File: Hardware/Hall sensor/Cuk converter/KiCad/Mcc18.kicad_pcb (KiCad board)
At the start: 2 copper layers, 202.2 x 107.2 mm, 47 parts, among them Q1 IRFP4321PbF, U1 LTSP_25-NP, U2 DRIVER_(INEP), U3 LM7812_TO220, U4 Signals_MCC, U5 ZCS

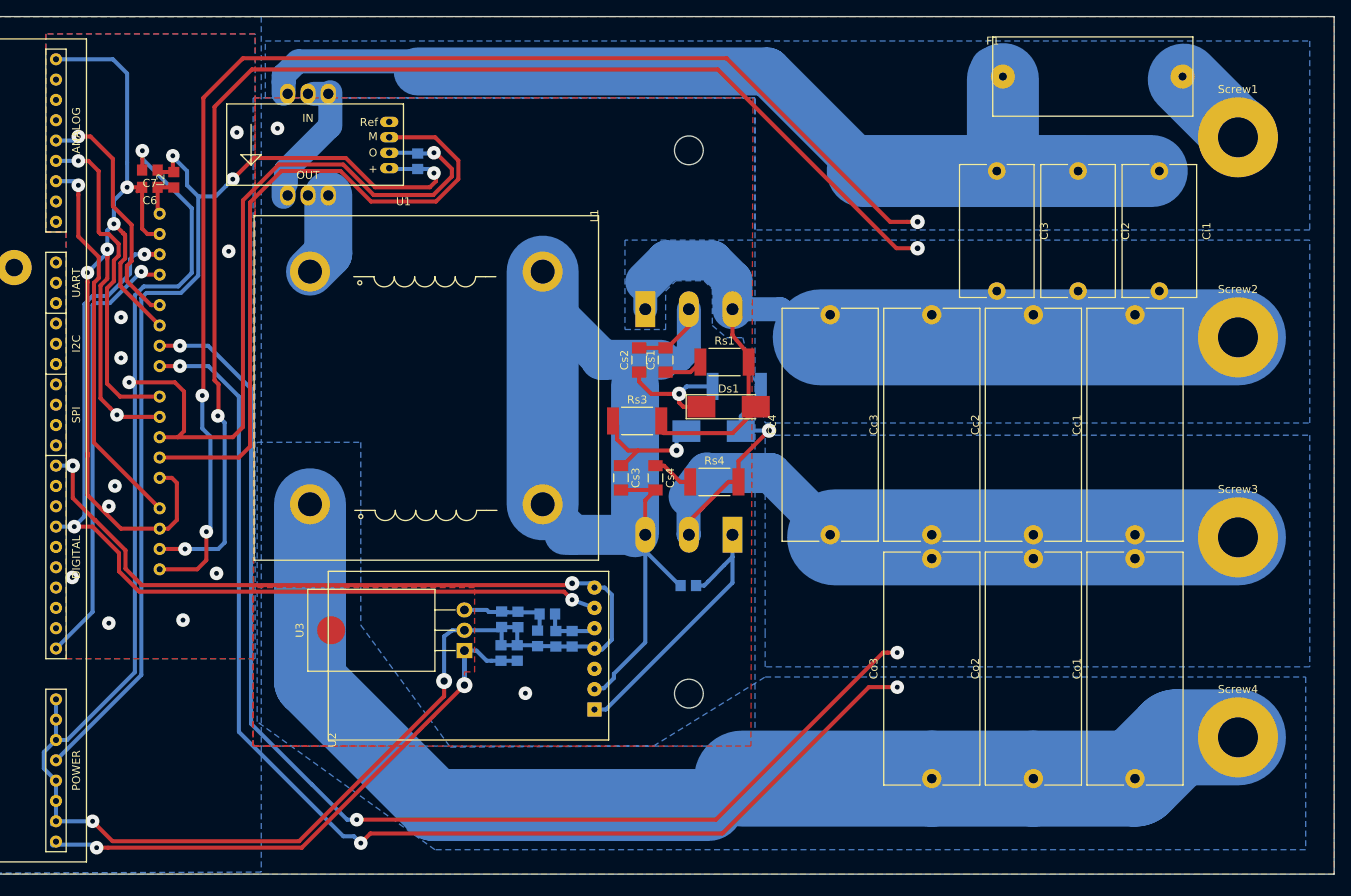
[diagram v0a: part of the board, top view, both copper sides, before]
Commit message: rework on snubber routing
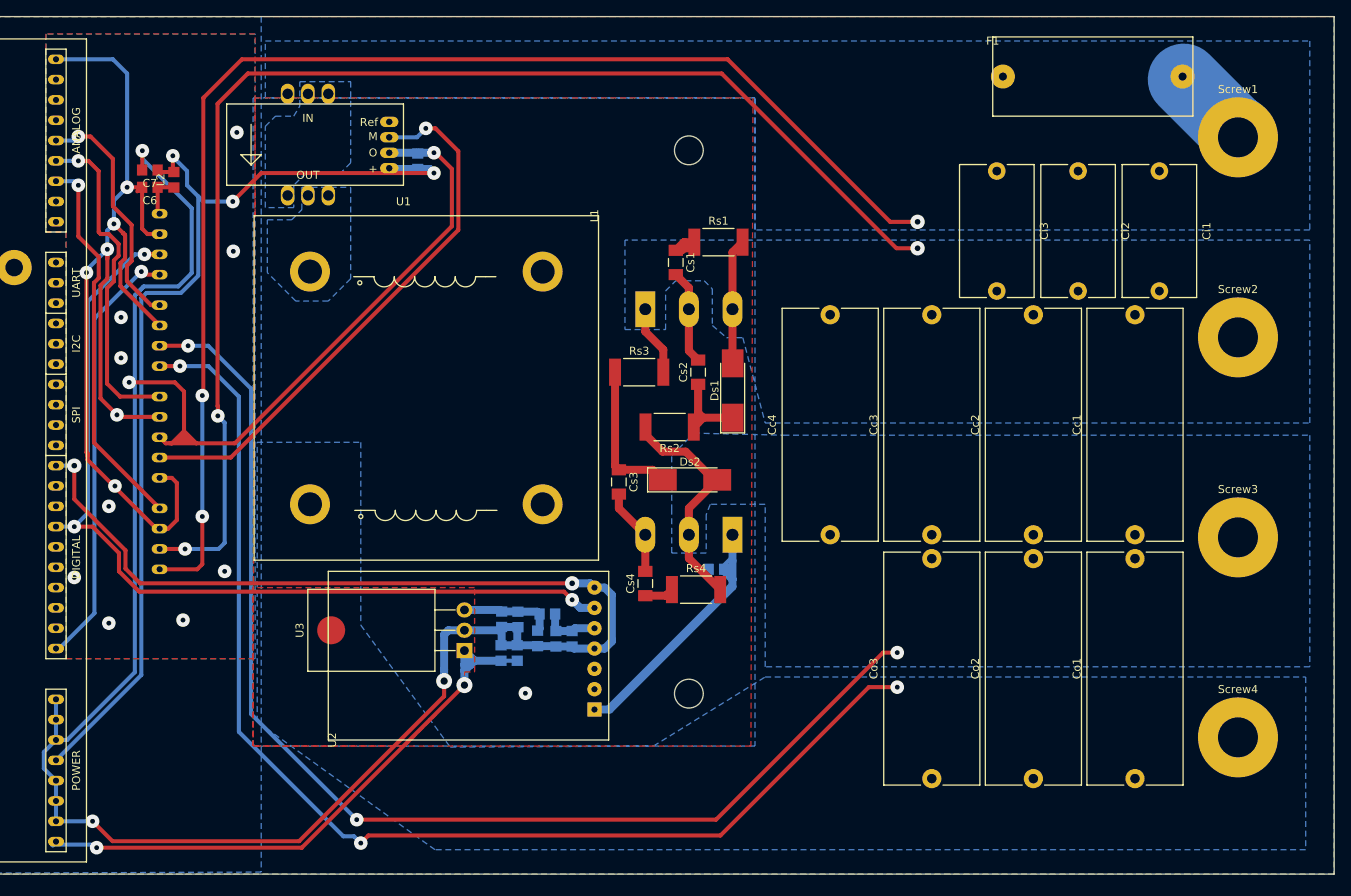
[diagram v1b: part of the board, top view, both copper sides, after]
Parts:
- Ds2, Rs2: moved to F.Cu
- moved HS1 54.6 mm to (208.3, 57.7)
- moved Rs1 15.0 mm to (210.1, 38.1)
- moved Rs4 13.7 mm to (207.3, 81.5)
- moved Cs4 13.3 mm to (200.9, 80.8), turned to 90 degrees
- moved Cs1 12.3 mm to (204.7, 40.6), turned to 270 degrees
- moved Rs2 9.80 mm to (204.0, 61.2), turned to 180 degrees
- moved Cs2 7.52 mm to (207.5, 54.4)
- moved Ds2 6.77 mm to (206.5, 67.8)
- moved Rs3 6.10 mm to (200.2, 54.4)
- moved R1 4.05 mm to (209.8, 79.0)
- moved Ds1 2.09 mm to (211.8, 56.6), turned to 90 degrees
- moved Cs3 0.57 mm to (197.6, 68.1)
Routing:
- net /+B: track 291.9 -> 149.5 mm
- net /-Vp: track 296.9 -> 164.0 mm
- net /Source: track 143.5 -> 22.9 mm, vias 2 -> 1
- net /+Vp: track 275.1 -> 186.3 mm
- net /-B: track 255.7 -> 178.3 mm, vias 4 -> 3
- net /Gate: track 35.9 -> 63.1 mm
- net Net-(U1-Pad3): track 16.2 -> 0.00 mm
- net /Ipanel+: track 84.9 -> 69.2 mm, vias 0 -> 1
- net Net-(L1-Pad1): track 10.5 -> 0.00 mm
- net Net-(Cs2-Pad1): track 15.5 -> 11.8 mm, vias 1 -> 0
- net Net-(Cs3-Pad1): track 15.6 -> 18.4 mm, vias 1 -> 0
- net +5V: track 132.3 -> 129.5 mm
- net /+18V_OUT: track 75.7 -> 78.3 mm
- net GNDA: track 140.4 -> 137.9 mm
- net Net-(Cs4-Pad1): track 5.19 -> 3.65 mm
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- added copper zone on B.Cu, net Net-(L1-Pad1)
- added copper zone on B.Cu, net Net-(U1-Pad3)

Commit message: PCB Reworked
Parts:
- added R101: ??, Resistor_SMD:R_0805_2012Metric_Pad1.29x1.40mm_HandSolder, F.Cu at (187.5, 65.5)
- added R102: ??, Resistor_SMD:R_0805_2012Metric_Pad1.29x1.40mm_HandSolder, F.Cu at (187.5, 68.8)
- added R103: ??, Resistor_SMD:R_0805_2012Metric_Pad1.29x1.40mm_HandSolder, F.Cu at (187.5, 123.4)
- added R104: ??, Resistor_SMD:R_0805_2012Metric_Pad1.29x1.40mm_HandSolder, F.Cu at (187.5, 120.1)
- added R105: 0R, Resistor_SMD:R_0805_2012Metric_Pad1.29x1.40mm_HandSolder, B.Cu at (141.2, 54.9)
- added R106: 0R, Resistor_SMD:R_0805_2012Metric_Pad1.29x1.40mm_HandSolder, B.Cu at (141.2, 56.9)
- moved HS1 103.6 mm to (147.1, 141.2)
- moved C2 52.5 mm to (145.7, 124.5), turned to 0 degrees
- moved L2 50.2 mm to (102.6, 61.5)
- moved C6 50.2 mm to (102.6, 65.8), turned to 270 degrees
- moved C3 49.3 mm to (145.7, 121.9), turned to 0 degrees
- moved C4 47.7 mm to (146.6, 116.0)
- moved C5 47.5 mm to (148.8, 116.0)
- moved C8 46.1 mm to (151.1, 116.0)
- moved Ds2 46.1 mm to (171.7, 98.0)
- moved R1 46.1 mm to (175.0, 109.2)
- moved C7 45.9 mm to (102.6, 57.1), turned to 90 degrees
- moved C1 45.9 mm to (137.7, 58.0)
- moved Rs2 45.9 mm to (169.2, 91.2)
- moved Screw4 45.9 mm to (240.2, 130.0)
- moved U3 45.9 mm to (143.5, 119.1)
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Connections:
- U1 pad 9: /Ipanel+ -> /+Ip
- U4 pad 1: /-Vp -> /Vp_sen-
- U4 pad 10: /+B -> /Vb_sen+
- U4 pad 11: /-B -> /Vb_sen-
- U4 pad 2: /+Vp -> /Vp_sen+
- U4 pad 6: /Ipanel+ -> /Ip_sen+
- U4 pad 7: GND -> /Ip_sen-
- U5 pad 2: GND -> Net-(U5-Pad2)
- U5 pad 4: GND -> Net-(U5-Pad4)
- U5 pad 6: GND -> Net-(U5-Pad6)
- U5 pad 8: GND -> Net-(U5-Pad8)
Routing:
- net /Vp_sen+: track 0.00 -> 172.4 mm
- net /Vp_sen-: track 0.00 -> 169.5 mm
- net /-Vp: track 164.0 -> 2.36 mm, vias 3 -> 1
- net /+Vp: track 186.3 -> 26.8 mm, vias 3 -> 1
- net /Vb_sen-: track 0.00 -> 153.6 mm, vias 0 -> 2
- net /Vb_sen+: track 0.00 -> 153.5 mm, vias 0 -> 2
- net /+B: track 149.5 -> 2.36 mm, vias 3 -> 1
- net /-B: track 178.3 -> 31.4 mm, vias 3 -> 1
- net GNDA: track 137.9 -> 2.92 mm, vias 15 -> 0
- net GND: track 377.7 -> 264.7 mm, vias 7 -> 10
- net /Ip_sen-: track 0.00 -> 94.5 mm, vias 0 -> 3
- net /Ip_sen+: track 0.00 -> 91.3 mm, vias 0 -> 3
- net /Ipanel+: track 69.2 -> 0.00 mm, vias 1 -> 0
- net +5V: track 129.5 -> 188.8 mm
- net +12V: track 11.8 -> 29.9 mm
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- added copper zone on F.Cu, net /+B
- added copper zone on F.Cu, net /+Vp
- added copper zone on F.Cu, net /-B
- added copper zone on F.Cu, net /-Vp
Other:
- board size 202.2 x 107.2 mm -> 199.1 x 107.2 mm
- rule via_min_size: 0.6 -> 0.7

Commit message: minor fixes and added IMG folder
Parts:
- moved R1 24.3 mm to (156.7, 125.2), turned to 270 degrees
- moved Cs4 3.06 mm to (169.2, 111.0)
- moved Rs4 3.05 mm to (175.5, 111.5)
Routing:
- net /Vp_sen-: track 169.5 -> 156.0 mm
- net /Gate: track 49.8 -> 40.7 mm
- net /Vp_sen+: track 172.4 -> 168.7 mm
- net /-B: track 31.4 -> 33.9 mm
- net /Source: track 22.9 -> 23.8 mm

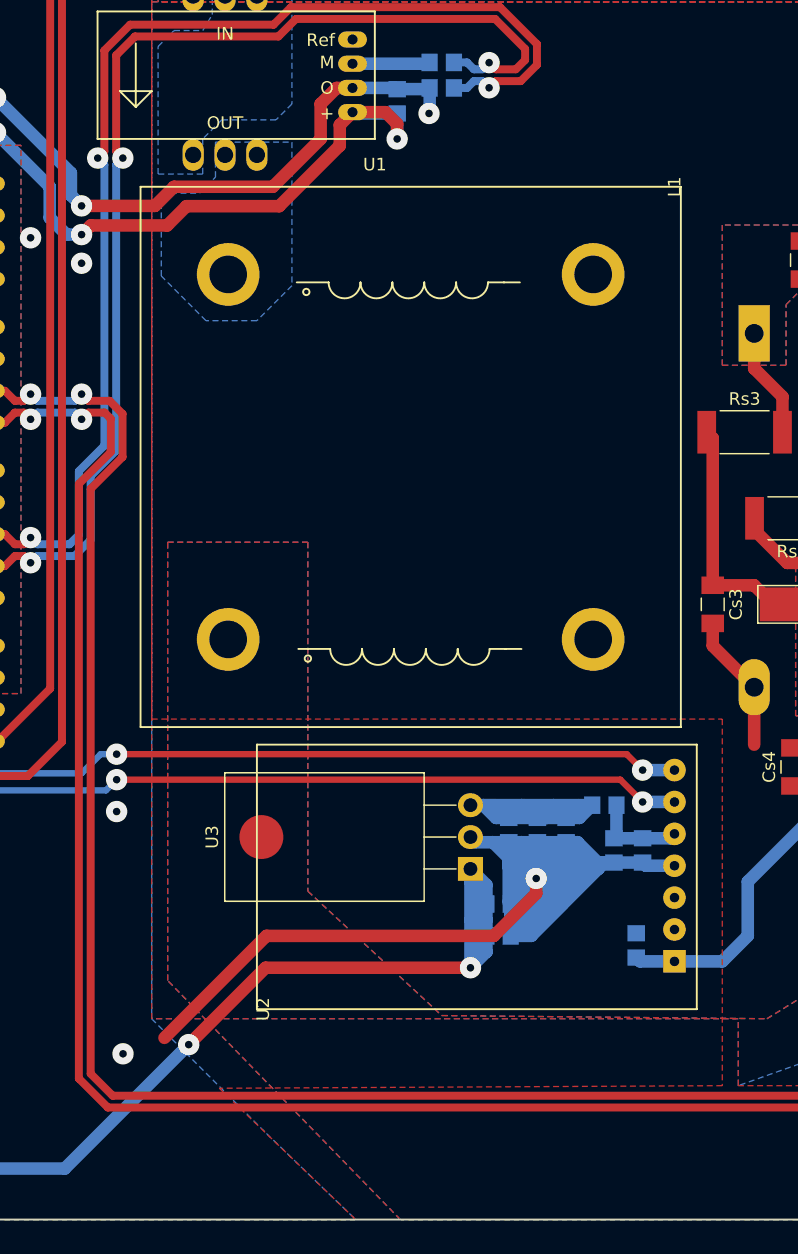
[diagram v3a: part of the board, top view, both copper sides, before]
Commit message: pads and traces of current sensor supply fixed
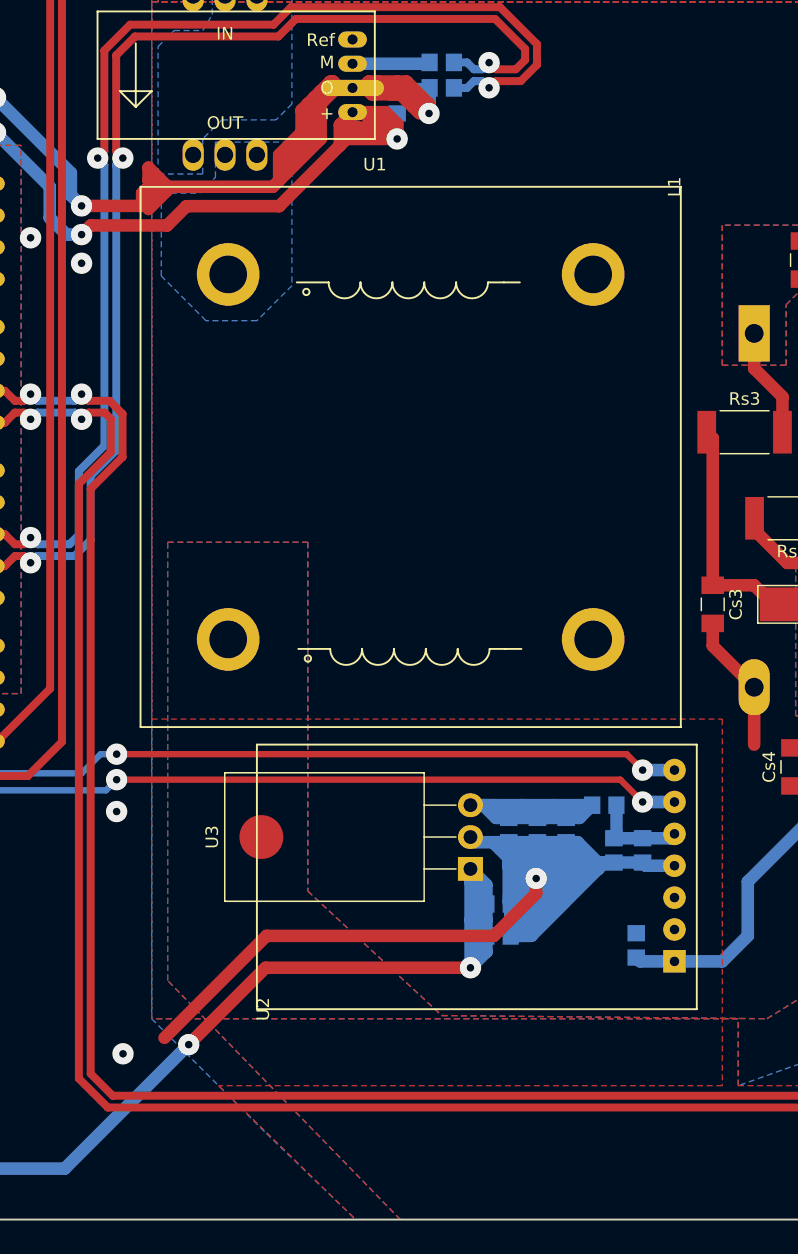
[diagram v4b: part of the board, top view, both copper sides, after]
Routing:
- net GND: track 264.7 -> 312.5 mm
- net +5V: track 188.8 -> 200.1 mm
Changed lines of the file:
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@@
     (thickness 1.6)
     (drawings 8)
-    (tracks 447)
+    (tracks 504)
     (zones 0)
     (modules 53)
@@
   )
   (setup
-    (last_trace_width 0.508)
+    (last_trace_width 1)
     (user_trace_width 0.508)
     (user_trace_width 0.8)
@@
     (mod_text_size 1 1)
     (mod_text_width 0.15)
-    (pad_size 1.7 2.54)
-    (pad_drill 1.3)
+    (pad_size 5 1.3)
+    (pad_drill 0.8)
     (pad_to_mask_clearance 0.2)
     (aux_axis_origin 50.038 39.878)
@@
     (pad 7 thru_hole oval (at 1.778 2.1336) (size 2.3 1.3) (drill 0.8) (layers *.Cu *.Mask)
       (net 3 +5V))
-    (pad 8 thru_hole oval (at 1.778 4.064) (size 2.3 1.3) (drill 0.8) (layers *.Cu *.Mask)
+    (pad 8 thru_hole oval (at 1.778 4.064) (size 5 1.3) (drill 0.8) (layers *.Cu *.Mask)
       (net 41 GND))
     (pad 9 thru_hole oval (at 1.778 5.9944) (size 2.3 1.3) (drill 0.8) (layers *.Cu *.Mask)
@@
   (segment (start 119.345189 67.852811) (end 120.8796 66.3184) (width 1) (layer F.Cu) (net 3))
   (segment (start 120.8796 66.3184) (end 128.27 66.3184) (width 1) (layer F.Cu) (net 3))
+  (segment (start 133.628398 60.960002) (end 133.096 61.4924) (width 1) (layer F.Cu) (net 3))
+  (segment (start 137.668 60.960002) (end 133.628398 60.960002) (width 1) (layer F.Cu) (net 3))
+  (segment (start 133.628398 60.960002) (end 133.628398 60.427602) (width 1) (layer F.Cu) (net 3))
+  (segment (start 133.628398 60.427602) (end 134.112 59.944) (width 1) (layer F.Cu) (net 3))
+  (segment (start 136.906 60.198) (end 136.906 60.452) (width 1) (layer F.Cu) (net 3))
+  (segment (start 136.652 59.944) (end 136.906 60.198) (width 1) (layer F.Cu) (net 3))
+  (segment (start 134.112 59.944) (end 136.906 60.452) (width 1) (layer F.Cu) (net 3))
+  (segment (start 136.906 60.198) (end 136.144 59.436) (width 1) (layer F.Cu) (net 3))
+  (segment (start 136.144 59.436) (end 135.382 59.436) (width 1) (layer F.Cu) (net 3))
   (segment (start 146.558 115.062) (end 148.844 115.062) (width 1) (layer B.Cu) (net 4) (status 30))
   (segment (start 152.1945 115.062) (end 153.2105 114.046) (width 1) (layer B.Cu) (net 4) (status 20))
@@
   (via (at 115.316 114.554) (size 1.7) (drill 0.6) (layers F.Cu B.Cu) (net 41))
   (segment (start 157.226 111.252) (end 159.766 111.252) (width 1) (layer B.Cu) (net 41) (status 20))
-  (segment (start 132.842 56.896) (end 134.112 56.896) (width 1) (layer F.Cu) (net 41) (status 20))
-  (segment (start 112.522 66.294) (end 118.364 66.294) (width 1) (layer F.Cu) (net 41))
-  (segment (start 118.364 66.294) (end 119.888 64.77) (width 1) (layer F.Cu) (net 41))
-  (segment (start 119.888 64.77) (end 127.762 64.77) (width 1) (layer F.Cu) (net 41))
-  (segment (start 131.572 60.96) (end 131.572 58.166) (width 1) (layer F.Cu) (net 41))
-  (segment (start 127.762 64.77) (end 131.572 60.96) (width 1) (layer F.Cu) (net 41))
-  (segment (start 131.572 58.166) (end 132.842 56.896) (width 1) (layer F.Cu) (net 41))
   (via (at 108.458 68.834) (size 1.7) (drill 0.6) (layers F.Cu B.Cu) (net 41))
   (via (at 112.522 70.866) (size 1.7) (drill 0.6) (layers F.Cu B.Cu) (net 41))
+  (segment (start 134.112 56.896) (end 135.128 56.896) (width 1) (layer F.Cu) (net 41))
+  (segment (start 135.128 56.896) (end 135.636 57.404) (width 1) (layer F.Cu) (net 41))
+  (segment (start 137.922 57.404) (end 138.43 57.912) (width 1) (layer F.Cu) (net 41))
+  (segment (start 138.43 57.912) (end 138.938 58.42) (width 1) (layer F.Cu) (net 41))
+  (segment (start 138.938 58.42) (end 139.446 58.928) (width 1) (layer F.Cu) (net 41))
+  (segment (start 138.43 56.388) (end 140.208 58.166) (width 1) (layer F.Cu) (net 41))
+  (segment (start 134.112 56.896) (end 134.874 56.896) (width 1) (layer F.Cu) (net 41))
+  (segment (start 140.208 58.166) (end 140.208 58.928) (width 1) (layer F.Cu) (net 41))
+  (segment (start 134.874 56.896) (end 135.382 56.388) (width 1) (layer F.Cu) (net 41))
+  (segment (start 140.208 58.928) (end 138.43 57.15) (width 1) (layer F.Cu) (net 41))
+  (segment (start 136.144 56.388) (end 136.144 57.15) (width 1) (layer F.Cu) (net 41))
+  (segment (start 135.636 57.404) (end 135.89 57.404) (width 1) (layer F.Cu) (net 41))
+  (segment (start 136.144 57.15) (end 135.89 57.404) (width 1) (layer F.Cu) (net 41))
+  (segment (start 135.382 56.388) (end 136.144 56.388) (width 1) (layer F.Cu) (net 41))
+  (segment (start 136.144 57.15) (end 136.906 57.15) (width 1) (layer F.Cu) (net 41))
+  (segment (start 136.906 57.15) (end 137.16 57.404) (width 1) (layer F.Cu) (net 41))
+  (segment (start 135.89 57.404) (end 137.16 57.404) (width 1) (layer F.Cu) (net 41))
+  (segment (start 137.16 57.404) (end 137.414 57.404) (width 1) (layer F.Cu) (net 41))
+  (segment (start 137.668 56.388) (end 137.668 57.404) (width 1) (layer F.Cu) (net 41))
+  (segment (start 137.668 57.404) (end 137.922 57.404) (width 1) (layer F.Cu) (net 41))
+  (segment (start 137.414 57.404) (end 137.668 57.404) (width 1) (layer F.Cu) (net 41))
+  (segment (start 136.144 56.388) (end 137.668 56.388) (width 1) (layer F.Cu) (net 41))
+  (segment (start 137.668 56.388) (end 138.43 56.388) (width 1) (layer F.Cu) (net 41))
+  (segment (start 131.572 58.166) (end 132.842 56.896) (width 1) (layer F.Cu) (net 41))
+  (segment (start 132.842 56.896) (end 134.112 56.896) (width 1) (layer F.Cu) (net 41) (status 20))
+  (segment (start 131.572 60.96) (end 131.572 58.166) (width 1) (layer F.Cu) (net 41))
+  (segment (start 133.096 56.896) (end 134.112 56.896) (width 1) (layer F.Cu) (net 41))
+  (segment (start 132.334 56.388) (end 132.588 56.388) (width 1) (layer F.Cu) (net 41))
+  (segment (start 132.588 56.388) (end 133.096 56.896) (width 1) (layer F.Cu) (net 41))
+  (segment (start 131.572 57.15) (end 132.334 56.388) (width 1) (layer F.Cu) (net 41))
+  (segment (start 131.064 57.658) (end 131.064 60.706) (width 1) (layer F.Cu) (net 41))
+  (segment (start 128.27 64.262) (end 128.27 62.23) (width 1) (layer F.Cu) (net 41))
+  (segment (start 128.27 64.262) (end 131.572 60.96) (width 1) (layer F.Cu) (net 41))
+  (segment (start 130.556 59.944) (end 130.556 60.96) (width 1) (layer F.Cu) (net 41))
+  (segment (start 130.556 60.96) (end 128.778 62.738) (width 1) (layer F.Cu) (net 41))
+  (segment (start 130.048 60.452) (end 130.048 58.674) (width 1) (layer F.Cu) (net 41))
+  (segment (start 128.27 62.23) (end 130.048 60.452) (width 1) (layer F.Cu) (net 41))
+  (segment (start 130.048 60.452) (end 130.556 59.944) (width 1) (layer F.Cu) (net 41))
+  (segment (start 130.556 58.166) (end 130.556 59.944) (width 1) (layer F.Cu) (net 41))
+  (segment (start 130.048 58.674) (end 130.556 58.166) (width 1) (layer F.Cu) (net 41))
+  (segment (start 130.556 58.166) (end 131.064 57.658) (width 1) (layer F.Cu) (net 41))
+  (segment (start 127.762 64.77) (end 128.27 64.262) (width 1) (layer F.Cu) (net 41))
+  (segment (start 117.348 65.278) (end 117.856 64.77) (width 1) (layer F.Cu) (net 41))
+  (segment (start 112.522 66.294) (end 117.348 66.294) (width 1) (layer F.Cu) (net 41))
+  (segment (start 117.348 66.294) (end 117.348 65.278) (width 1) (layer F.Cu) (net 41))
+  (segment (start 119.38 64.77) (end 127.762 64.77) (width 1) (layer F.Cu) (net 41))
+  (segment (start 119.38 65.024) (end 117.856 66.548) (width 1) (layer F.Cu) (net 41))
+  (segment (start 119.38 65.024) (end 119.38 64.77) (width 1) (layer F.Cu) (net 41))
+  (segment (start 119.38 64.77) (end 117.856 63.246) (width 1) (layer F.Cu) (net 41))
+  (segment (start 117.856 64.262) (end 118.364 64.77) (width 1) (layer F.Cu) (net 41))
+  (segment (start 117.856 63.246) (end 117.856 64.262) (width 1) (layer F.Cu) (net 41))
+  (segment (start 117.856 64.77) (end 118.364 64.77) (width 1) (layer F.Cu) (net 41))
+  (segment (start 119.38 64.77) (end 118.872 64.77) (width 1) (layer F.Cu) (net 41))
+  (segment (start 118.872 64.77) (end 118.11 65.532) (width 1) (layer F.Cu) (net 41))
+  (segment (start 131.572 57.15) (end 131.064 57.658) (width 1) (layer F.Cu) (net 41))
   (segment (start 144.78 125.73) (end 144.78 123.19) (width 1) (layer B.Cu) (net 42))
   (segment (start 144.78 123.19) (end 143.51 123.19) (width 1) (layer B.Cu) (net 42))
@@
     (polygon
       (pts
-        (xy 118.11 107.188) (xy 163.576 107.188) (xy 163.576 136.398) (xy 123.495664 136.60354) (xy 134.366 147.066)
+        (xy 118.11 107.188) (xy 163.576 107.188) (xy 163.576 136.398) (xy 123.444 136.398) (xy 134.366 147.066)
         (xy 50.038 147.066) (xy 50.038 39.878) (xy 118.11 39.878)
       )

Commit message: minor fixes
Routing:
- net Net-(Cs3-Pad1): track 18.4 -> 40.7 mm
- net /Vp_sen-: track 156.0 -> 166.0 mm
- net /-Vp: vias 1 -> 5
- net /+B: vias 1 -> 5
